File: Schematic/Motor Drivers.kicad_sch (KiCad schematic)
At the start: 16 parts, among them U26 DRV8243SQDGQRQ1 (S-Variant), U27 DRV8243SQDGQRQ1 (S-Variant)

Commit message: Added DigiKey to BOM
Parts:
- C126, C127: DigiKey Link (none) -> https://www.digikey.com/short/2nhzzz3n; DigiKey Part Number (none) -> CL10B104MB8NNNC; DigiKey Price per Unit (none) -> 0.08; Link https://mou.sr/3JWJm45 -> (none); Manufactaurer Part Number (none) -> CL10B104MB8NNNC; Manufacturer Part Number CL10B104MB8NNNC -> (none); Mouser Link (none) -> https://mou.sr/3JWJm45; Mouser Part Number (none) -> 187-CL10B104MB8NNNC; Mouser Price per Unit (none) -> 0.10; Price per Unit 0.10 -> (none); Supplier Mouser -> (none); Supplier Part Number 187-CL10B104MB8NNNC -> (none)
- D29, D30: DigiKey Link (none) -> https://www.digikey.com/short/7pp2m58h; DigiKey Part Number (none) -> 516-ASMM-CR03-BU802TR-ND; DigiKey Price per Unit (none) -> 0.32; Link https://mou.sr/460BFB7 -> (none); Manufactaurer Part Number (none) -> ASMM-CR03-BU802; Manufacturer Part Number ASMM-CR03-BU802 -> (none); Mouser Link (none) -> https://mou.sr/460BFB7; Mouser Part Number (none) -> 630-ASMM-CR03-BU802; Mouser Price per Unit (none) -> 0.32; Price per Unit 0.32 -> (none); Supplier Mouser -> (none); Supplier Part Number 630-ASMM-CR03-BU802 -> (none)
- R92, R93: DigiKey Link (none) -> https://www.digikey.com/short/0wt4qm7j; DigiKey Part Number (none) -> 541-2792-2-ND; DigiKey Price per Unit (none) -> 0.13; Link https://mou.sr/48a41vp -> (none); Manufactaurer Part Number (none) -> RCS06034K70FKEA; Manufacturer Part Number RCS06034K70FKEA -> (none); Mouser Link (none) -> https://mou.sr/48a41vp; Mouser Part Number (none) -> 71-RCS06034K70FKEA; Mouser Price per Unit (none) -> 0.13; Price per Unit 0.13 -> (none); Supplier Mouser -> (none); Supplier Part Number 71-RCS06034K70FKEA -> (none)
- R95: DigiKey Link (none) -> https://www.digikey.com/short/0zttpzn7; DigiKey Part Number (none) -> 408-RG1608P-331-D-T5TR-ND; DigiKey Price per Unit (none) -> 0.10; Link https://mou.sr/4m95jdp -> (none); Manufactaurer Part Number (none) -> RG1608P-331-D-T5; Manufacturer Part Number RG1608P-331-D-T5 -> (none); Mouser Link (none) -> https://mou.sr/4m95jdp; Mouser Part Number (none) -> 754-RG1608P-331DT5; Mouser Price per Unit (none) -> 0.10; Price per Unit 0.10 -> (none); Supplier Mouser -> (none); Supplier Part Number 754-RG1608P-331DT5 -> (none)
- R96: DigiKey Link (none) -> N/A; DigiKey Part Number (none) -> N/A; DigiKey Price per Unit (none) -> N/A; Link https://mou.sr/46iPyuQ -> (none); Manufactaurer Part Number (none) -> RMC1/16K8200FTP; Manufacturer Part Number RMC1/16K8200FTP -> (none); Mouser Link (none) -> https://mou.sr/46iPyuQ; Mouser Part Number (none) -> 791-RMC1/16K8200FTP; Mouser Price per Unit (none) -> 0.10; Price per Unit 0.10 -> (none); Supplier Mouser -> (none); Supplier Part Number 791-RMC1/16K8200FTP -> (none)
- U26, U27: DigiKey Link (none) -> https://www.digikey.com/short/vfzd222r; DigiKey Part Number (none) -> 296-DRV8243SQDGQRQ1TR-ND; DigiKey Price per Unit (none) -> 4.72; Manufactaurer Part Number (none) -> DRV8243SQDGQRQ1; Mouser Link (none) -> https://mou.sr/4nrRg3N; Mouser Part Number (none) -> 595-DRV8243SQDGQRQ1; Mouser Price per Unit (none) -> 6.37

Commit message: need to do Qs now
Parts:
- C126, C127: DigiKey Part Number CL10B104MB8NNNC -> (none)
- D31: renamed from D29; DigiKey Part Number 516-ASMM-CR03-BU802TR-ND -> (none)
- D32: renamed from D30; DigiKey Part Number 516-ASMM-CR03-BU802TR-ND -> (none)
- R92, R93: DigiKey Part Number 541-2792-2-ND -> (none)
- R95: DigiKey Part Number 408-RG1608P-331-D-T5TR-ND -> (none)
- U24: renamed from U26; DigiKey Part Number 296-DRV8243SQDGQRQ1TR-ND -> (none)
- U25: renamed from U27; DigiKey Part Number 296-DRV8243SQDGQRQ1TR-ND -> (none)
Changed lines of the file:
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@@
 			)
 		)
-		(property "DigiKey Part Number" "CL10B104MB8NNNC"
+		(property "DigiKey Part Number" ""
 			(at 68.58 55.88 0)
 			(effects
@@
 			)
 		)
-		(property "DigiKey Part Number" "408-RG1608P-331-D-T5TR-ND"
+		(property "DigiKey Part Number" ""
 			(at 215.9 31.75 90)
 			(effects
@@
 		(on_board yes)
 		(dnp no)
-		(property "Reference" "U27"
+		(property "Reference" "U25"
 			(at 159.258 29.21 0)
 			(effects
@@
 			)
 		)
-		(property "DigiKey Part Number" "296-DRV8243SQDGQRQ1TR-ND"
+		(property "DigiKey Part Number" ""
 			(at 118.11 34.29 0)
 			(effects
@@
 			(project "STAR"
 				(path "/fc8533bc-25dd-4c20-9b4c-ffebebd6739b/f73d6367-f3ba-42df-a3ea-bd155f1c219f/07712c52-f5ae-4a00-8c08-8de30640eab9"
-					(reference "U27")
+					(reference "U25")
 					(unit 1)
 				)
@@
 		(on_board yes)
 		(dnp no)
-		(property "Reference" "U26"
+		(property "Reference" "U24"
 			(at 156.718 97.79 0)
 			(effects
@@
 			)
 		)
-		(property "DigiKey Part Number" "296-DRV8243SQDGQRQ1TR-ND"
+		(property "DigiKey Part Number" ""
 			(at 115.57 102.87 0)
 			(effects
@@
 			(project "STAR"
 				(path "/fc8533bc-25dd-4c20-9b4c-ffebebd6739b/f73d6367-f3ba-42df-a3ea-bd155f1c219f/07712c52-f5ae-4a00-8c08-8de30640eab9"
-					(reference "U26")
+					(reference "U24")
 					(unit 1)
 				)
@@
 		(on_board yes)
 		(dnp no)
-		(property "Reference" "D30"
+		(property "Reference" "D32"
 			(at 224.79 30.734 0)
 			(effects
@@
 			)
 		)
-		(property "DigiKey Part Number" "516-ASMM-CR03-BU802TR-ND "
+		(property "DigiKey Part Number" ""
 			(at 229.87 31.75 0)
 			(effects
@@
 			(project "STAR"
 				(path "/fc8533bc-25dd-4c20-9b4c-ffebebd6739b/f73d6367-f3ba-42df-a3ea-bd155f1c219f/07712c52-f5ae-4a00-8c08-8de30640eab9"
-					(reference "D30")
+					(reference "D32")
 					(unit 1)
 				)
@@
 			)
 		)
-		(property "DigiKey Part Number" "541-2792-2-ND"
+		(property "DigiKey Part Number" ""
 			(at 203.2 105.41 0)
 			(effects
@@
 			)
 		)
-		(property "DigiKey Part Number" "CL10B104MB8NNNC"
+		(property "DigiKey Part Number" ""
 			(at 66.04 124.46 0)
 			(effects
@@
 		(on_board yes)
 		(dnp no)
-		(property "Reference" "D29"
+		(property "Reference" "D31"
 			(at 222.25 99.314 0)
 			(effects
@@
 			)
 		)
-		(property "DigiKey Part Number" "516-ASMM-CR03-BU802TR-ND "
+		(property "DigiKey Part Number" ""
 			(at 227.33 100.33 0)
 			(effects
@@
 			(project "STAR"
 				(path "/fc8533bc-25dd-4c20-9b4c-ffebebd6739b/f73d6367-f3ba-42df-a3ea-bd155f1c219f/07712c52-f5ae-4a00-8c08-8de30640eab9"
-					(reference "D29")
+					(reference "D31")
 					(unit 1)
 				)
@@
 			)
 		)
-		(property "DigiKey Part Number" "541-2792-2-ND"
+		(property "DigiKey Part Number" ""
 			(at 204.47 36.83 0)
 			(effects

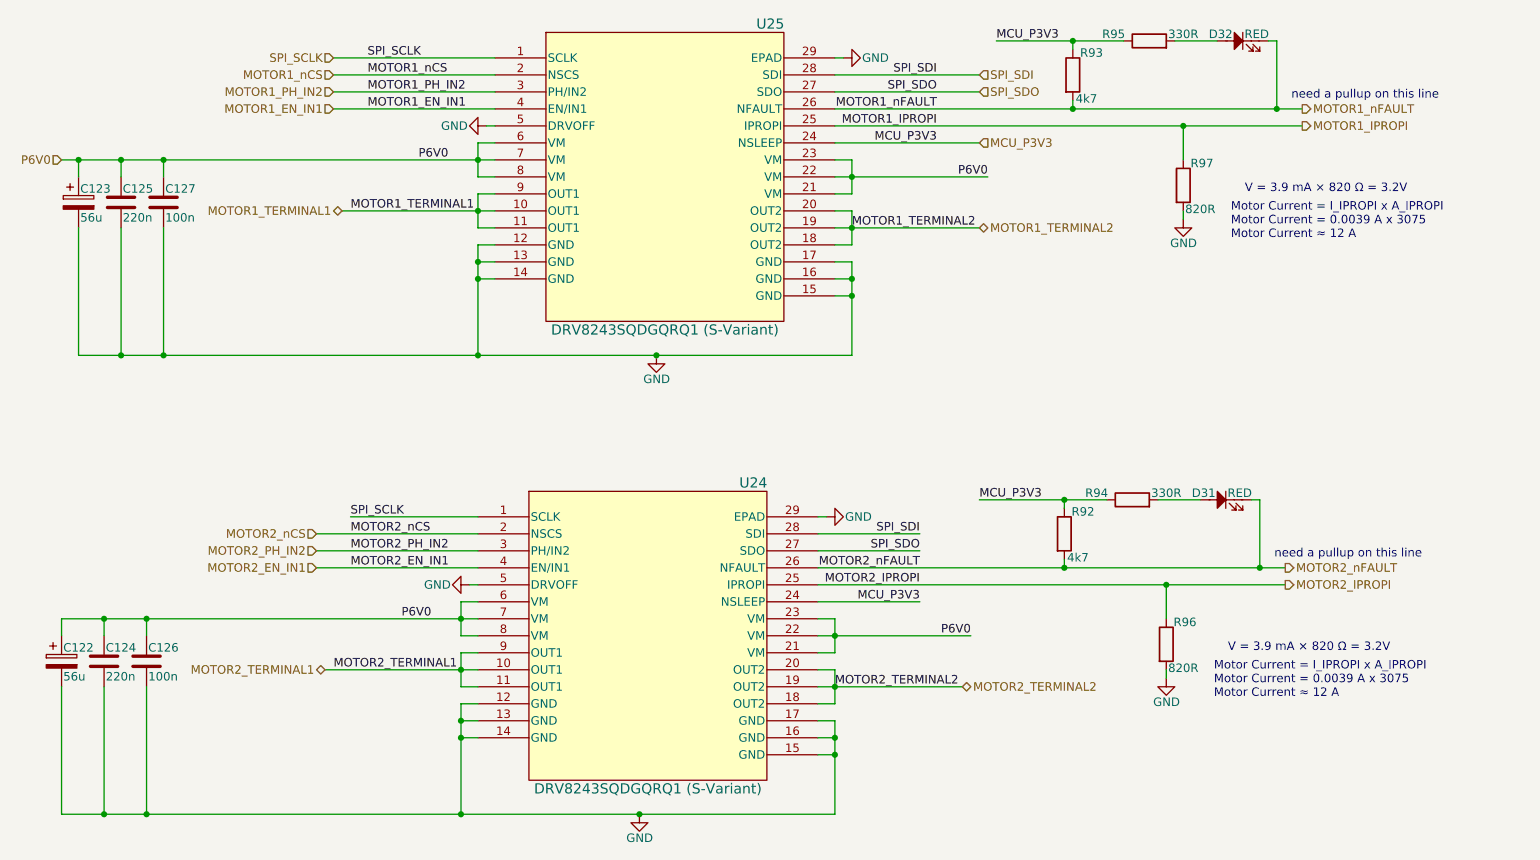
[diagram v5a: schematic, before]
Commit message: Added fuse, more footprints, and cleaned up some things
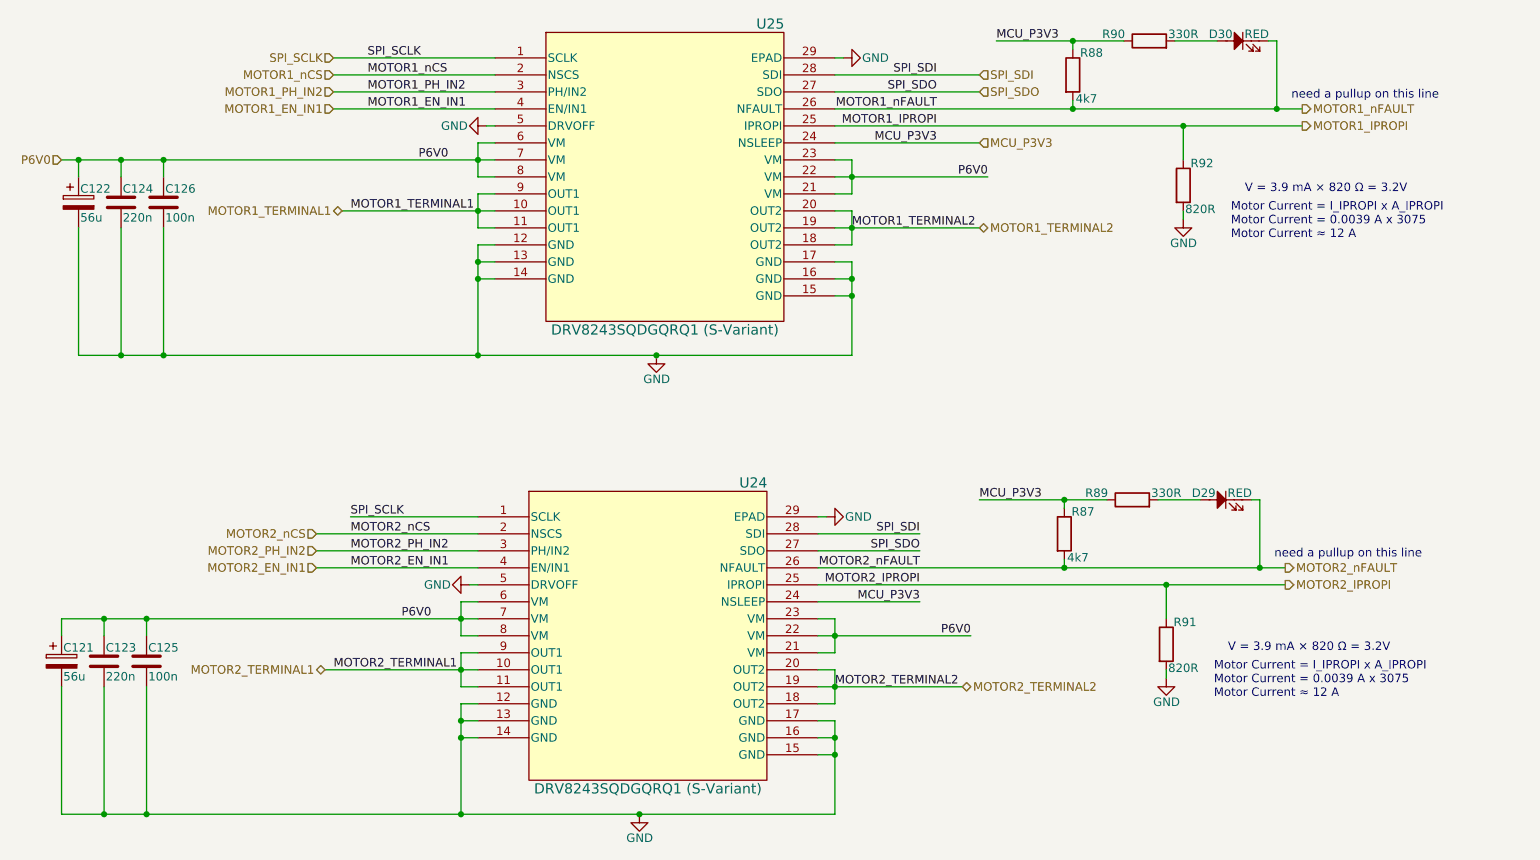
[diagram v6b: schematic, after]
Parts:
- renumbered C122 to C121, C123 to C122, C124 to C123, C125 to C124, C126 to C125, C127 to C126, D31 to D29, D32 to D30, R92 to R87, R93 to R88, R94 to R89, R95 to R90, R96 to R91, R97 to R92
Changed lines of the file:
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@@
 		(on_board yes)
 		(dnp no)
-		(property "Reference" "C127"
+		(property "Reference" "C126"
 			(at 68.834 53.848 0)
 			(effects
@@
 			(project "STAR"
 				(path "/fc8533bc-25dd-4c20-9b4c-ffebebd6739b/f73d6367-f3ba-42df-a3ea-bd155f1c219f/07712c52-f5ae-4a00-8c08-8de30640eab9"
-					(reference "C127")
+					(reference "C126")
 					(unit 1)
 				)
@@
 		(on_board yes)
 		(dnp no)
-		(property "Reference" "R94"
+		(property "Reference" "R89"
 			(at 208.026 99.314 90)
 			(effects
@@
 			(project "STAR"
 				(path "/fc8533bc-25dd-4c20-9b4c-ffebebd6739b/f73d6367-f3ba-42df-a3ea-bd155f1c219f/07712c52-f5ae-4a00-8c08-8de30640eab9"
-					(reference "R94")
+					(reference "R89")
 					(unit 1)
 				)
@@
 		(on_board yes)
 		(dnp no)
-		(property "Reference" "#PWR068"
+		(property "Reference" "#PWR065"
 			(at 110.49 44.45 0)
 			(effects
@@
 			(project "STAR"
 				(path "/fc8533bc-25dd-4c20-9b4c-ffebebd6739b/f73d6367-f3ba-42df-a3ea-bd155f1c219f/07712c52-f5ae-4a00-8c08-8de30640eab9"
-					(reference "#PWR068")
+					(reference "#PWR065")
 					(unit 1)
 				)
@@
 		(on_board yes)
 		(dnp no)
-		(property "Reference" "#PWR071"
+		(property "Reference" "#PWR068"
 			(at 173.99 102.87 0)
 			(effects
@@
 			(project "STAR"
 				(path "/fc8533bc-25dd-4c20-9b4c-ffebebd6739b/f73d6367-f3ba-42df-a3ea-bd155f1c219f/07712c52-f5ae-4a00-8c08-8de30640eab9"
-					(reference "#PWR071")
+					(reference "#PWR068")
 					(unit 1)
 				)
@@
 		(on_board yes)
 		(dnp no)
-		(property "Reference" "R95"
+		(property "Reference" "R90"
 			(at 210.566 30.734 90)
 			(effects
@@
 			(project "STAR"
 				(path "/fc8533bc-25dd-4c20-9b4c-ffebebd6739b/f73d6367-f3ba-42df-a3ea-bd155f1c219f/07712c52-f5ae-4a00-8c08-8de30640eab9"
-					(reference "R95")
+					(reference "R90")
 					(unit 1)
 				)
@@
 		(on_board yes)
 		(dnp no)
-		(property "Reference" "#PWR072"
+		(property "Reference" "#PWR069"
 			(at 176.53 34.29 0)
 			(effects
@@
 			(project "STAR"
 				(path "/fc8533bc-25dd-4c20-9b4c-ffebebd6739b/f73d6367-f3ba-42df-a3ea-bd155f1c219f/07712c52-f5ae-4a00-8c08-8de30640eab9"
-					(reference "#PWR072")
+					(reference "#PWR069")
 					(unit 1)
 				)
@@
 		(on_board yes)
 		(dnp no)
-		(property "Reference" "C125"
+		(property "Reference" "C124"
 			(at 62.484 53.848 0)
 			(effects
@@
 			(project "STAR"
 				(path "/fc8533bc-25dd-4c20-9b4c-ffebebd6739b/f73d6367-f3ba-42df-a3ea-bd155f1c219f/07712c52-f5ae-4a00-8c08-8de30640eab9"
-					(reference "C125")
+					(reference "C124")
 					(unit 1)
 				)
@@
 		(on_board yes)
 		(dnp no)
-		(property "Reference" "C123"
+		(property "Reference" "C122"
 			(at 56.134 53.848 0)
 			(effects
@@
 			(project "STAR"
 				(path "/fc8533bc-25dd-4c20-9b4c-ffebebd6739b/f73d6367-f3ba-42df-a3ea-bd155f1c219f/07712c52-f5ae-4a00-8c08-8de30640eab9"
-					(reference "C123")
+					(reference "C122")
 					(unit 1)
 				)
@@
 		(on_board yes)
 		(dnp no)
-		(property "Reference" "C122"
+		(property "Reference" "C121"
 			(at 53.594 122.428 0)
 			(effects
@@
 			(project "STAR"
 				(path "/fc8533bc-25dd-4c20-9b4c-ffebebd6739b/f73d6367-f3ba-42df-a3ea-bd155f1c219f/07712c52-f5ae-4a00-8c08-8de30640eab9"
-					(reference "C122")
+					(reference "C121")
 					(unit 1)
 				)
@@
 		(on_board yes)
 		(dnp no)
-		(property "Reference" "R97"
+		(property "Reference" "R92"
 			(at 223.774 50.038 0)
 			(effects
@@
 			(project "STAR"
 				(path "/fc8533bc-25dd-4c20-9b4c-ffebebd6739b/f73d6367-f3ba-42df-a3ea-bd155f1c219f/07712c52-f5ae-4a00-8c08-8de30640eab9"
-					(reference "R97")
+					(reference "R92")
 					(unit 1)
 				)
@@
 		(on_board yes)
 		(dnp no)
-		(property "Reference" "D32"
+		(property "Reference" "D30"
 			(at 224.79 30.734 0)
 			(effects
@@
 			(project "STAR"
 				(path "/fc8533bc-25dd-4c20-9b4c-ffebebd6739b/f73d6367-f3ba-42df-a3ea-bd155f1c219f/07712c52-f5ae-4a00-8c08-8de30640eab9"
-					(reference "D32")
+					(reference "D30")
 					(unit 1)
 				)
@@
 		(on_board yes)
 		(dnp no)
-		(property "Reference" "R92"
+		(property "Reference" "R87"
 			(at 205.994 102.108 0)
 			(effects
@@
 			(project "STAR"
 				(path "/fc8533bc-25dd-4c20-9b4c-ffebebd6739b/f73d6367-f3ba-42df-a3ea-bd155f1c219f/07712c52-f5ae-4a00-8c08-8de30640eab9"
-					(reference "R92")
+					(reference "R87")
 					(unit 1)
 				)
@@
 		(on_board yes)
 		(dnp no)
-		(property "Reference" "#PWR069"
+		(property "Reference" "#PWR066"
 			(at 139.7 153.67 0)
 			(effects
@@
 			(project "STAR"
 				(path "/fc8533bc-25dd-4c20-9b4c-ffebebd6739b/f73d6367-f3ba-42df-a3ea-bd155f1c219f/07712c52-f5ae-4a00-8c08-8de30640eab9"
-					(reference "#PWR069")
+					(reference "#PWR066")
 					(unit 1)
 				)
@@
 		(on_board yes)
 		(dnp no)
-		(property "Reference" "C126"
+		(property "Reference" "C125"
 			(at 66.294 122.428 0)
 			(effects
@@
 			(project "STAR"
 				(path "/fc8533bc-25dd-4c20-9b4c-ffebebd6739b/f73d6367-f3ba-42df-a3ea-bd155f1c219f/07712c52-f5ae-4a00-8c08-8de30640eab9"
-					(reference "C126")
+					(reference "C125")
 					(unit 1)
 				)
@@
 		(on_board yes)
 		(dnp no)
-		(property "Reference" "#PWR074"
+		(property "Reference" "#PWR071"
 			(at 220.98 64.77 0)
 			(effects
@@
 			(project "STAR"
 				(path "/fc8533bc-25dd-4c20-9b4c-ffebebd6739b/f73d6367-f3ba-42df-a3ea-bd155f1c219f/07712c52-f5ae-4a00-8c08-8de30640eab9"
-					(reference "#PWR074")
+					(reference "#PWR071")
 					(unit 1)
 				)
@@
 		(on_board yes)
 		(dnp no)
-		(property "Reference" "#PWR067"
+		(property "Reference" "#PWR064"
 			(at 107.95 113.03 0)
 			(effects
@@
 			(project "STAR"
 				(path "/fc8533bc-25dd-4c20-9b4c-ffebebd6739b/f73d6367-f3ba-42df-a3ea-bd155f1c219f/07712c52-f5ae-4a00-8c08-8de30640eab9"
-					(reference "#PWR067")
+					(reference "#PWR064")
 					(unit 1)
 				)
@@
 		(on_board yes)
 		(dnp no)
-		(property "Reference" "C124"
+		(property "Reference" "C123"
 			(at 59.944 122.428 0)
 			(effects
@@
 			(project "STAR"
 				(path "/fc8533bc-25dd-4c20-9b4c-ffebebd6739b/f73d6367-f3ba-42df-a3ea-bd155f1c219f/07712c52-f5ae-4a00-8c08-8de30640eab9"
-					(reference "C124")
+					(reference "C123")
 					(unit 1)
 				)
@@
 		(on_board yes)
 		(dnp no)
-		(property "Reference" "D31"
+		(property "Reference" "D29"
 			(at 222.25 99.314 0)
 			(effects
@@
 			(project "STAR"
 				(path "/fc8533bc-25dd-4c20-9b4c-ffebebd6739b/f73d6367-f3ba-42df-a3ea-bd155f1c219f/07712c52-f5ae-4a00-8c08-8de30640eab9"
-					(reference "D31")
+					(reference "D29")
 					(unit 1)
 				)
@@
 		(on_board yes)
 		(dnp no)
-		(property "Reference" "#PWR073"
+		(property "Reference" "#PWR070"
 			(at 218.44 133.35 0)
 			(effects
@@
 			(project "STAR"
 				(path "/fc8533bc-25dd-4c20-9b4c-ffebebd6739b/f73d6367-f3ba-42df-a3ea-bd155f1c219f/07712c52-f5ae-4a00-8c08-8de30640eab9"
-					(reference "#PWR073")
+					(reference "#PWR070")
 					(unit 1)
 				)
@@
 		(on_board yes)
 		(dnp no)
-		(property "Reference" "R96"
+		(property "Reference" "R91"
 			(at 221.234 118.618 0)
 			(effects
@@
 			(project "STAR"
 				(path "/fc8533bc-25dd-4c20-9b4c-ffebebd6739b/f73d6367-f3ba-42df-a3ea-bd155f1c219f/07712c52-f5ae-4a00-8c08-8de30640eab9"
-					(reference "R96")
+					(reference "R91")
 					(unit 1)
 				)
@@
 		(on_board yes)
 		(dnp no)
-		(property "Reference" "R93"
+		(property "Reference" "R88"
 			(at 207.264 33.528 0)
 			(effects
@@
 			(project "STAR"
 				(path "/fc8533bc-25dd-4c20-9b4c-ffebebd6739b/f73d6367-f3ba-42df-a3ea-bd155f1c219f/07712c52-f5ae-4a00-8c08-8de30640eab9"
-					(reference "R93")
+					(reference "R88")
 					(unit 1)
 				)
@@
 		(on_board yes)
 		(dnp no)
-		(property "Reference" "#PWR070"
+		(property "Reference" "#PWR067"
 			(at 142.24 85.09 0)
 			(effects
@@
 			(project "STAR"
 				(path "/fc8533bc-25dd-4c20-9b4c-ffebebd6739b/f73d6367-f3ba-42df-a3ea-bd155f1c219f/07712c52-f5ae-4a00-8c08-8de30640eab9"
-					(reference "#PWR070")
+					(reference "#PWR067")
 					(unit 1)
 				)
